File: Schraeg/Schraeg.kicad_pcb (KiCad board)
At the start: 2 copper layers, 84.5 x 128.5 mm, 116 parts, among them U1 TL074, U2 TL074, U3 V2164, U4 TL074, U5 TL074

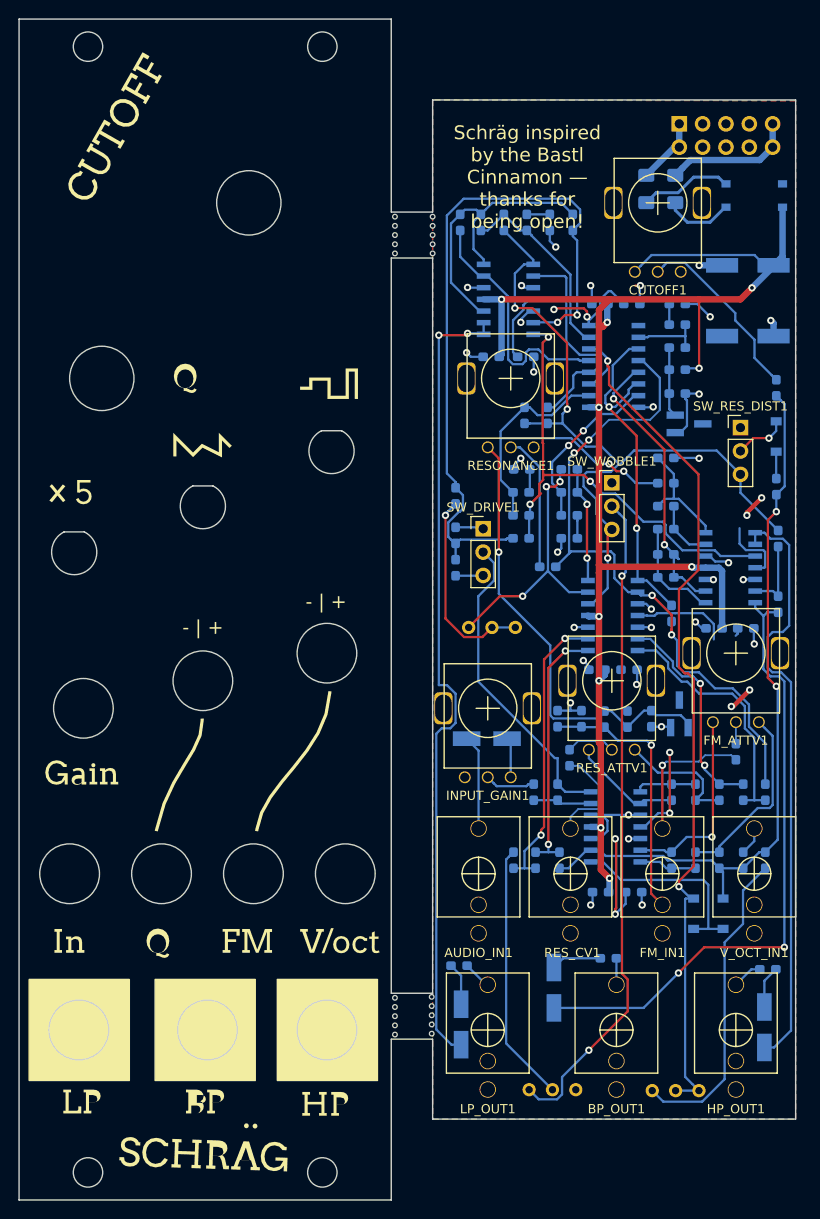
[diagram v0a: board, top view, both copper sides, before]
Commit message: fixes filter schematic
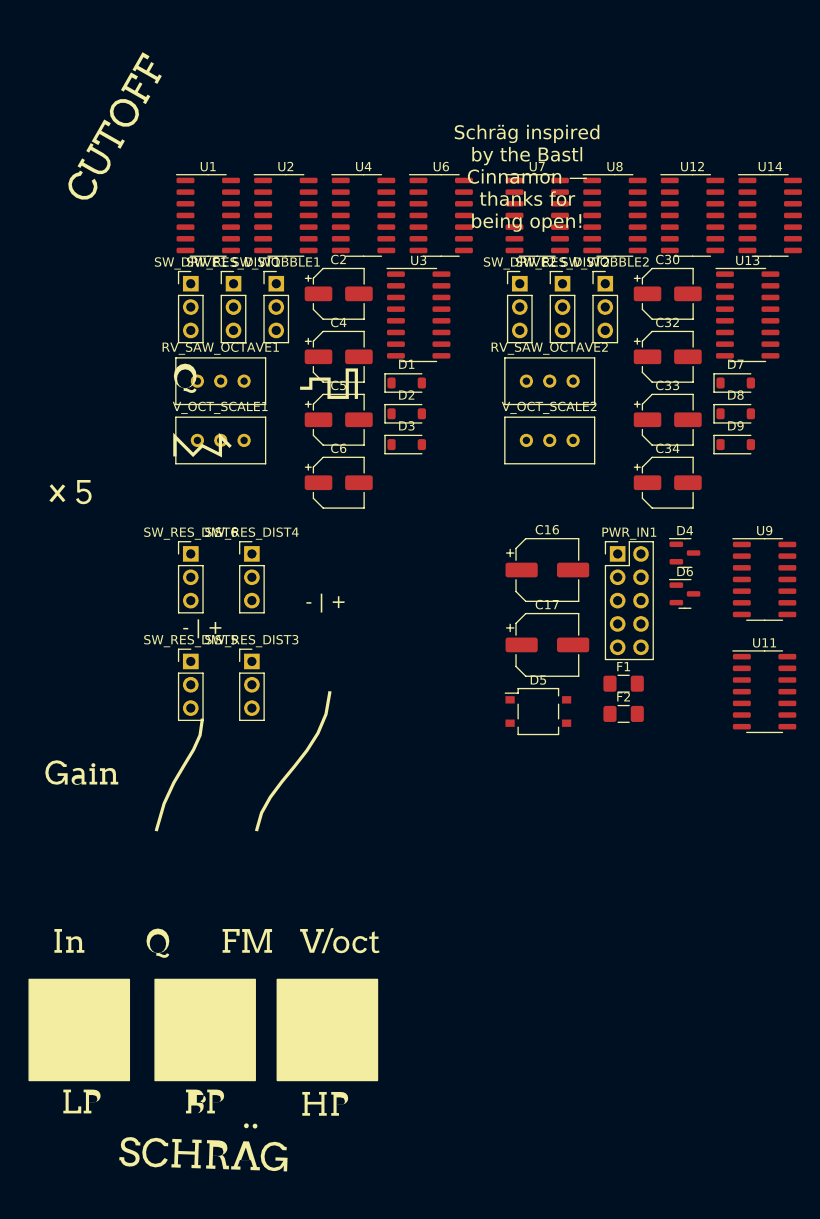
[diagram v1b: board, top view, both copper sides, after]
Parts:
- removed AUDIO_IN1, BP_OUT1, FM_IN1, HP_OUT1, LP_OUT1, RES_CV1, V_OCT_IN1: PJ301M-12, Eurocad:PJ301M-12
- removed C1, C12, C7, C8: 560pF, Capacitor_SMD:C_0603_1608Metric_Pad1.05x0.95mm_HandSolder
- removed C10, C11, C13: 220pF, Capacitor_SMD:C_0603_1608Metric_Pad1.05x0.95mm_HandSolder
- removed C14, C15, C18: 220n, Capacitor_SMD:C_0603_1608Metric_Pad1.05x0.95mm_HandSolder
- removed C19, C20, C21, C22, C23, C24, C25, C26, C27, C28: 100n, Capacitor_SMD:C_0603_1608Metric_Pad1.05x0.95mm_HandSolder
- removed C3, C9: 100pF, Capacitor_SMD:C_0603_1608Metric_Pad1.05x0.95mm_HandSolder
- removed CUTOFF1, FM_ATTV1, INPUT_GAIN1, RESONANCE1, RES_ATTV1: 100k, Eurocad:Alpha9mmPot
- removed MOUSEBITE1mm (x4): VAL**, Eurocad:MOUSEBITE1mm
- removed R1, R10, R11, R12, R13, R16, R17, R2, R20, R3, R4, R5, R6, R7, R8, R9: 100k, Resistor_SMD:R_0603_1608Metric_Pad1.05x0.95mm_HandSolder
- removed R14, R40: 15K, Resistor_SMD:R_0603_1608Metric_Pad1.05x0.95mm_HandSolder
- removed R15, R30, R32, R39: 470R, Resistor_SMD:R_0603_1608Metric_Pad1.05x0.95mm_HandSolder
- removed R18: 22k, Resistor_SMD:R_0603_1608Metric_Pad1.05x0.95mm_HandSolder
- removed R19, R22: 47k, Resistor_SMD:R_0603_1608Metric_Pad1.05x0.95mm_HandSolder
- removed R21: 10k, Resistor_SMD:R_0603_1608Metric_Pad1.05x0.95mm_HandSolder
- removed R23, R24, R25: 1K, Resistor_SMD:R_0603_1608Metric_Pad1.05x0.95mm_HandSolder
- removed R26: 330K, Resistor_SMD:R_0603_1608Metric_Pad1.05x0.95mm_HandSolder
- removed R27, R28, R29, R31, R33, R34, R35, R36, R38: 33k, Resistor_SMD:R_0603_1608Metric_Pad1.05x0.95mm_HandSolder
- removed R37, R42, R45, R48, R49: 100K, Resistor_SMD:R_0603_1608Metric_Pad1.05x0.95mm_HandSolder
- removed R41: 1.5K, Resistor_SMD:R_0603_1608Metric_Pad1.05x0.95mm_HandSolder
- removed R43: 470K, Resistor_SMD:R_0603_1608Metric_Pad1.05x0.95mm_HandSolder
- removed R44, R47: 6.8K, Resistor_SMD:R_0603_1608Metric_Pad1.05x0.95mm_HandSolder
- removed R46: 3.3K, Resistor_SMD:R_0603_1608Metric_Pad1.05x0.95mm_HandSolder
- removed RES_ADJ1: 250K, Potentiometer_THT:Potentiometer_Bourns_3296W_Vertical
- removed Ref** (x2): Val**, Schraeg:Schraeg Panel Graphics Inkscape
- removed U5: TL074, Package_SO:SOIC-14_3.9x8.7mm_P1.27mm
- added C30: 10uF, Capacitor_SMD:CP_Elec_5x4.5, F.Cu at (70.6, 29.9)
- added C32: 10uF, Capacitor_SMD:CP_Elec_5x4.5, F.Cu at (70.6, 36.8)
- added C33: 10uF, Capacitor_SMD:CP_Elec_5x4.5, F.Cu at (70.6, 43.6)
- added C34: 10uF, Capacitor_SMD:CP_Elec_5x4.5, F.Cu at (70.6, 50.5)
- added D7: D_Small, Diode_SMD:D_SOD-123, F.Cu at (78.0, 39.6)
- added D8: D_Small, Diode_SMD:D_SOD-123, F.Cu at (78.0, 43.0)
- added D9: 5V, Diode_SMD:D_SOD-123, F.Cu at (78.0, 46.3)
- added RV_SAW_OCTAVE2: 100k, Potentiometer_THT:Potentiometer_Bourns_3296W_Vertical, F.Cu at (60.3, 39.4)
- added SW_DRIVE2: SW_SPDT, Connector_PinHeader_2.54mm:PinHeader_1x03_P2.54mm_Vertical, F.Cu at (54.5, 28.8)
- added SW_RES_DIST2: SW_SPDT, Connector_PinHeader_2.54mm:PinHeader_1x03_P2.54mm_Vertical, F.Cu at (59.1, 28.8)
- added SW_RES_DIST3: SW_SPDT, Connector_PinHeader_2.54mm:PinHeader_1x03_P2.54mm_Vertical, F.Cu at (25.3, 69.9)
- added SW_RES_DIST4: SW_SPDT, Connector_PinHeader_2.54mm:PinHeader_1x03_P2.54mm_Vertical, F.Cu at (25.3, 58.2)
- added SW_RES_DIST5: SW_SPDT, Connector_PinHeader_2.54mm:PinHeader_1x03_P2.54mm_Vertical, F.Cu at (18.7, 69.9)
- added SW_RES_DIST6: SW_SPDT, Connector_PinHeader_2.54mm:PinHeader_1x03_P2.54mm_Vertical, F.Cu at (18.7, 58.2)
- added SW_WOBBLE2: SW_SPDT, Connector_PinHeader_2.54mm:PinHeader_1x03_P2.54mm_Vertical, F.Cu at (63.8, 28.8)
- added U11: TL074, Package_SO:SOIC-14_3.9x8.7mm_P1.27mm, F.Cu at (81.1, 73.2)
- added U12: TL074, Package_SO:SOIC-14_3.9x8.7mm_P1.27mm, F.Cu at (73.3, 21.4)
- added U13: V2164, Package_SO:SOIC-16_3.9x9.9mm_P1.27mm, F.Cu at (79.3, 32.2)
- added U14: TL074, Package_SO:SOIC-14_3.9x8.7mm_P1.27mm, F.Cu at (81.7, 21.4)
- added U6: TL074, Package_SO:SOIC-14_3.9x8.7mm_P1.27mm, F.Cu at (45.9, 21.4)
- added U7: TL074, Package_SO:SOIC-14_3.9x8.7mm_P1.27mm, F.Cu at (56.4, 21.4)
- added U8: TL074, Package_SO:SOIC-14_3.9x8.7mm_P1.27mm, F.Cu at (64.8, 21.4)
- added U9: TL074, Package_SO:SOIC-14_3.9x8.7mm_P1.27mm, F.Cu at (81.1, 61.0)
- added V_OCT_SCALE2: 5K, Potentiometer_THT:Potentiometer_Bourns_3296W_Vertical, F.Cu at (60.3, 45.9)
- C16, C17, C2, C4, C5, C6, D1, D2, D3, D5, F1, F2, PWR_IN1, RV_SAW_OCTAVE1, U1, U2, U3, U4, V_OCT_SCALE1: moved to F.Cu
- D4, D6: footprint Package_TO_SOT_SMD:SOT-23_Handsoldering -> Package_TO_SOT_SMD:SOT-23; moved to F.Cu
- moved C4 86.4 mm to (34.8, 36.8), turned to 0 degrees
- moved V_OCT_SCALE1 83.5 mm to (24.5, 45.9), turned to 0 degrees
- moved RV_SAW_OCTAVE1 83.1 mm to (24.5, 39.4), turned to 0 degrees
- moved U1 79.9 mm to (20.6, 21.4), turned to 0 degrees
- moved D1 67.2 mm to (42.2, 39.6), turned to 0 degrees
- moved C5 66.1 mm to (34.8, 43.6), turned to 0 degrees
- moved D2 62.7 mm to (42.2, 43.0), turned to 0 degrees
- moved D5 60.9 mm to (56.5, 75.3)
- moved C6 60.4 mm to (34.8, 50.5), turned to 0 degrees
- moved F2 57.4 mm to (65.8, 75.6), turned to 0 degrees
- moved SW_RES_DIST1 57.3 mm to (23.3, 28.8)
- moved U2 56.2 mm to (29.0, 21.4), turned to 0 degrees
- moved U4 55.3 mm to (37.5, 21.4), turned to 0 degrees
- moved F1 53.9 mm to (65.8, 72.3), turned to 0 degrees
- moved C2 51.0 mm to (34.8, 29.9)
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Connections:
- net Net-(D1-Pad2) renamed /Left Channel/FM_CV_IN
- C2 pad 1: Net-(AUDIO_IN1-Pad3) -> /Left Channel/AUDIO_IN
- C4 pad 1: /Filter Core/HP_OUT -> /Left Channel/HP_OUT
- C5 pad 1: /Filter Core/BP_OUT -> /Left Channel/BP_OUT
- C6 pad 1: /Filter Core/LP_OUT -> /Left Channel/LP_OUT
- D2 pad 1: /Filter Core/FREQ_CV -> /Left Channel/FREQ_CV
- SW_RES_DIST1 pad 1: (no net) -> unconnected-(SW_RES_DIST1-A-Pad1)
- SW_RES_DIST1 pad 3: /Filter Core/RES_MOD -> /Left Channel/RES_MOD
- SW_WOBBLE1 pad 1: (no net) -> unconnected-(SW_WOBBLE1-A-Pad1)
- SW_WOBBLE1 pad 3: /Filter Core/RES_MOD -> /Left Channel/RES_MOD
- U1 pad 1: Net-(R3-Pad1) -> (no net)
- U1 pad 2: Net-(R3-Pad2) (its old number) -> (no net)
- U1 pad 3: GND -> (no net)
- U2 pad 1: /Filter Core/RES_CV -> (no net)
- U2 pad 12: /Filter Core/RES_MOD -> (no net)
- U2 pad 13: Net-(R27-Pad2) -> (no net)
- U2 pad 14: Net-(R27-Pad1) -> (no net)
- U2 pad 2: Net-(C3-Pad2) -> (no net)
- U2 pad 3: GND -> (no net)
- U2 pad 6: Net-(R11-Pad1) -> /Invert Switch A/CV_OUT
- U3 pad 1: (no net) -> unconnected-(U3E-MODE-Pad1)
- U3 pad 10: Net-(C10-Pad2) -> (no net)
- U3 pad 11: /Filter Core/FREQ_CV -> (no net)
- U3 pad 12: Net-(C11-Pad2) -> (no net)
- U3 pad 13: Net-(C13-Pad2) -> (no net)
- U3 pad 14: /Filter Core/FREQ_CV -> (no net)
- U3 pad 15: Net-(R38-Pad1) -> (no net)
- U3 pad 3: /Filter Core/RES_CV -> /Left Channel/RES_CV
- U3 pad 4: Net-(C3-Pad2) -> Net-(U4A--)
- U3 pad 5: Net-(C9-Pad2) -> (no net)
- U3 pad 6: /Filter Core/RES_CV -> (no net)
- U3 pad 7: Net-(R29-Pad1) -> (no net)
- U4 pad 1: /Filter Core/HP_OUT -> /Left Channel/RES_CV
- U4 pad 10: GND -> (no net)
- U4 pad 12: GND -> (no net)
- U4 pad 13: Net-(R35-Pad1) -> (no net)
- U4 pad 14: Net-(R36-Pad1) -> (no net)
- U4 pad 2: /Filter Core/HP_OUT -> Net-(U4A--)
- U4 pad 3: Net-(R28-Pad1) -> GND
- U4 pad 7: /Filter Core/BP_OUT -> Net-(SW_RES_DIST3-A)
- U4 pad 8: Net-(C9-Pad1) -> (no net)
- U4 pad 9: Net-(C9-Pad2) -> (no net)
- V_OCT_SCALE1 pad 2: /Filter Core/FREQ_CV -> /Left Channel/FREQ_CV
- V_OCT_SCALE1 pad 3: /Filter Core/FREQ_CV -> /Left Channel/FREQ_CV
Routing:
- net -12V: track 165.0 -> 0.00 mm, vias 10 -> 0
- net /Filter Core/FREQ_CV: track 97.1 -> 0.00 mm, vias 2 -> 0
- net /Filter Core/LP_OUT: track 87.9 -> 0.00 mm, vias 2 -> 0
- net /Filter Core/RES_MOD: track 83.3 -> 0.00 mm, vias 3 -> 0
- net /Left Channel/FM_CV_IN: track 80.0 -> 0.00 mm, vias 2 -> 0
- net /Filter Core/AUDIO_IN: track 78.7 -> 0.00 mm, vias 2 -> 0
- net GND: track 74.3 -> 0.00 mm, vias 32 -> 0
- net Net-(C3-Pad2): track 73.4 -> 0.00 mm, vias 4 -> 0
- net Net-(SW_WOBBLE1-B): track 72.2 -> 0.00 mm, vias 2 -> 0
- net /Filter Core/BP_OUT: track 68.9 -> 0.00 mm, vias 2 -> 0
- net +12V: track 65.9 -> 0.00 mm, vias 10 -> 0
- net /Filter Core/HP_OUT: track 65.2 -> 0.00 mm
- net Net-(R28-Pad1): track 52.1 -> 0.00 mm, vias 3 -> 0
- net 5V_REF: track 50.4 -> 0.00 mm, vias 1 -> 0
- net Net-(C10-Pad2): track 40.7 -> 0.00 mm, vias 2 -> 0
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- removed copper zone on B.Cu, net +12V
- removed copper zone on F.Cu, net GND
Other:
- board outline removed
- net class Default removed
- board text removed: "Power Either Way"
- board text removed: "Res. Adj."
- board text removed: "Saw Adj."
- board text removed: "Schräg v0.2.1 Barnaby Walters waterpigs.co.uk cc-by-sa 2021"
- board text removed: "V/oct Adj."
